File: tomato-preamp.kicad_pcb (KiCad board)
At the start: 2 copper layers, 77 x 75.6 mm, 25 parts, among them J1 IN, J2 OUT, J3.1 +ANODE, J3.2 -ANODE, J4.1 +HEATER, J4.2 -HEATER, U1 6N2P

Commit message: single-layer version
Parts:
- RV1, RV2: moved to B.Cu
- moved R8 25.0 mm to (168.8, 106.4), turned to -90 degrees
- moved C5 25.0 mm to (168.8, 101.3)
- moved C4 10.1 mm to (159.3, 89.7), turned to 180 degrees
- moved RV2 9.84 mm to (139.2, 62.3)
- moved RV1 9.80 mm to (159.8, 62.2)
- moved R6 6.49 mm to (159.4, 79.7)
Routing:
- net Net-(U1B-K): track 19.5 -> 34.2 mm
- net Net-(C6-Pad2): track 19.0 -> 11.9 mm
- net Net-(U1B-G): track 54.0 -> 61.0 mm
- net Net-(U1B-A): track 42.3 -> 45.4 mm
- net Net-(C3-Pad2): track 12.2 -> 10.5 mm
- net Net-(C4-Pad1): track 28.3 -> 27.7 mm
- net GND: vias 44 -> 34

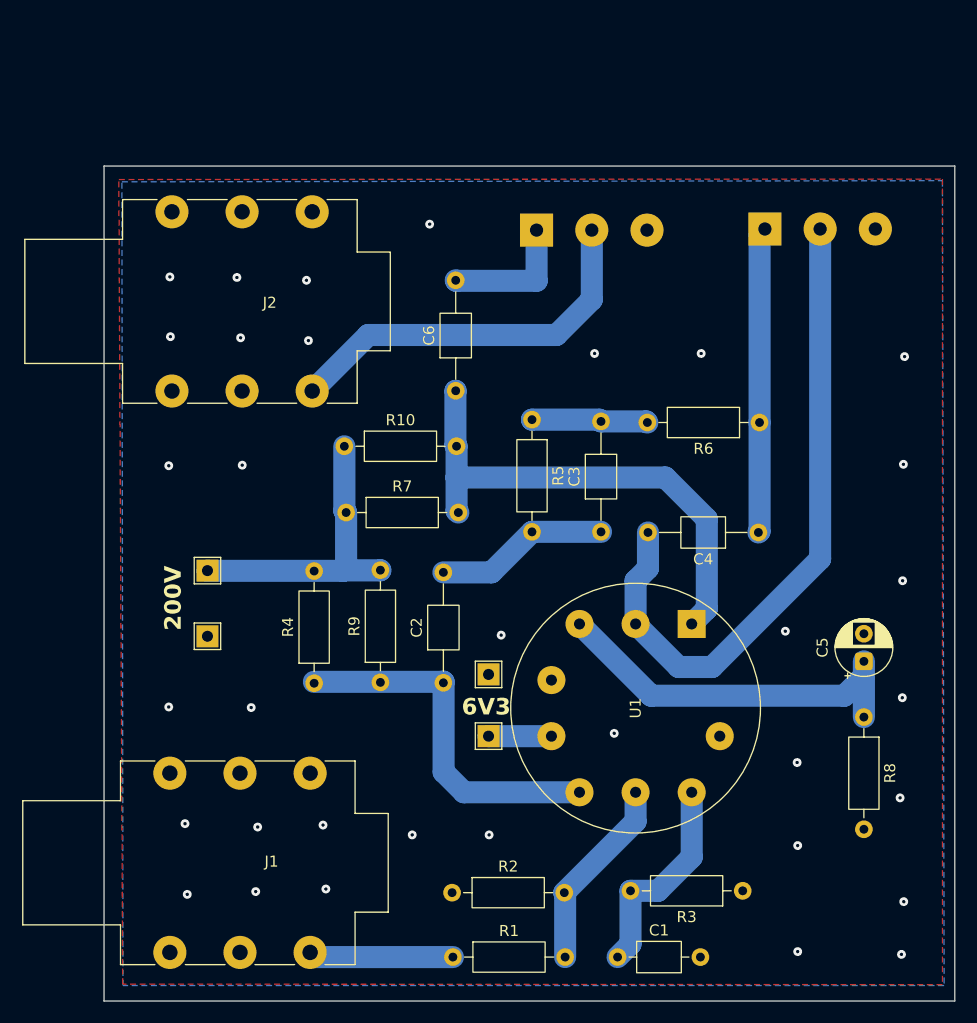
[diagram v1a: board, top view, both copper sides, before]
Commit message: moving potentiometers to the equidistant places
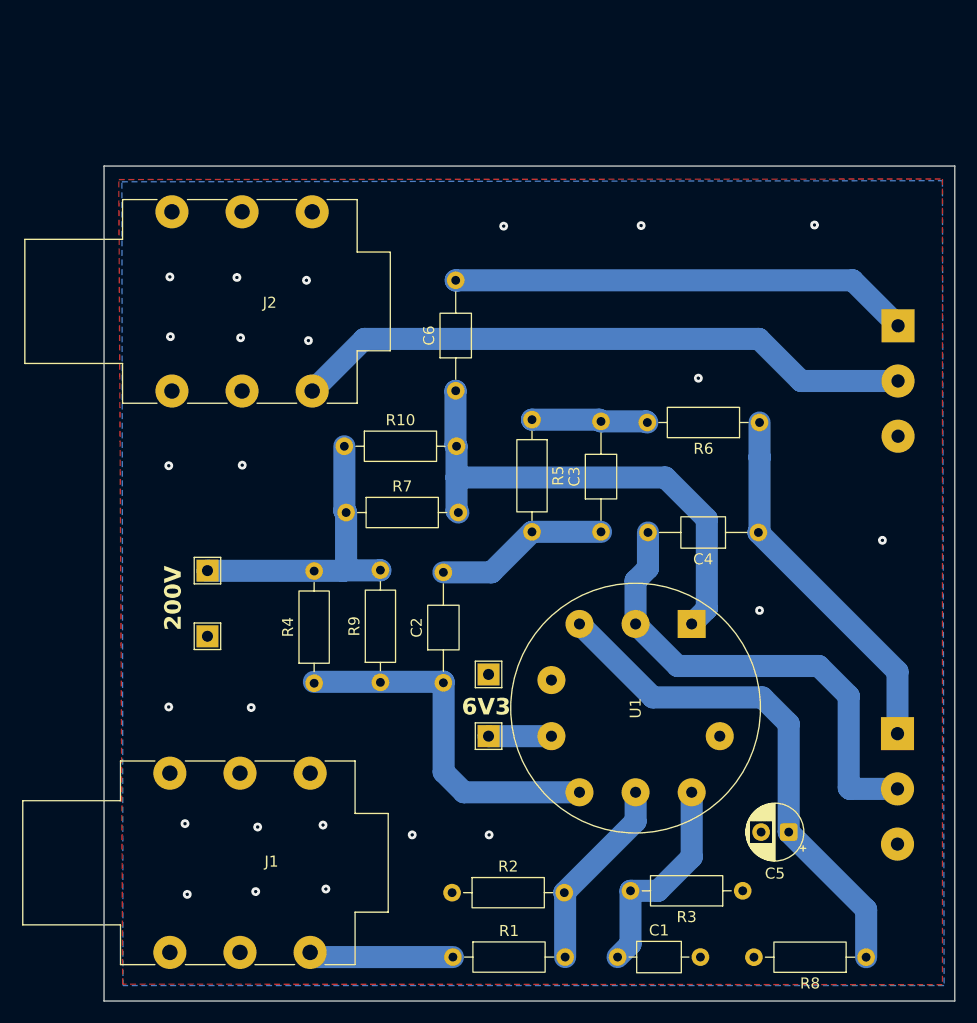
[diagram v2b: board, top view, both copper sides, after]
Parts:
- moved RV1 47.2 mm to (171.9, 107.9), turned to 180 degrees
- moved RV2 33.9 mm to (171.9, 70.9), turned to 180 degrees
- moved R8 21.7 mm to (169.0, 128.1), turned to 180 degrees
- moved C5 16.9 mm to (162.0, 116.8), turned to 180 degrees
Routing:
- net Net-(C6-Pad2): track 11.9 -> 41.8 mm
- net Net-(J2-PadT): track 35.0 -> 56.6 mm
- net Net-(U1B-G): track 61.0 -> 43.5 mm
- net Net-(U1B-K): track 34.2 -> 46.7 mm
- net Net-(C4-Pad1): track 27.7 -> 33.5 mm
- net GND: vias 34 -> 24

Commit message: shorten the traces
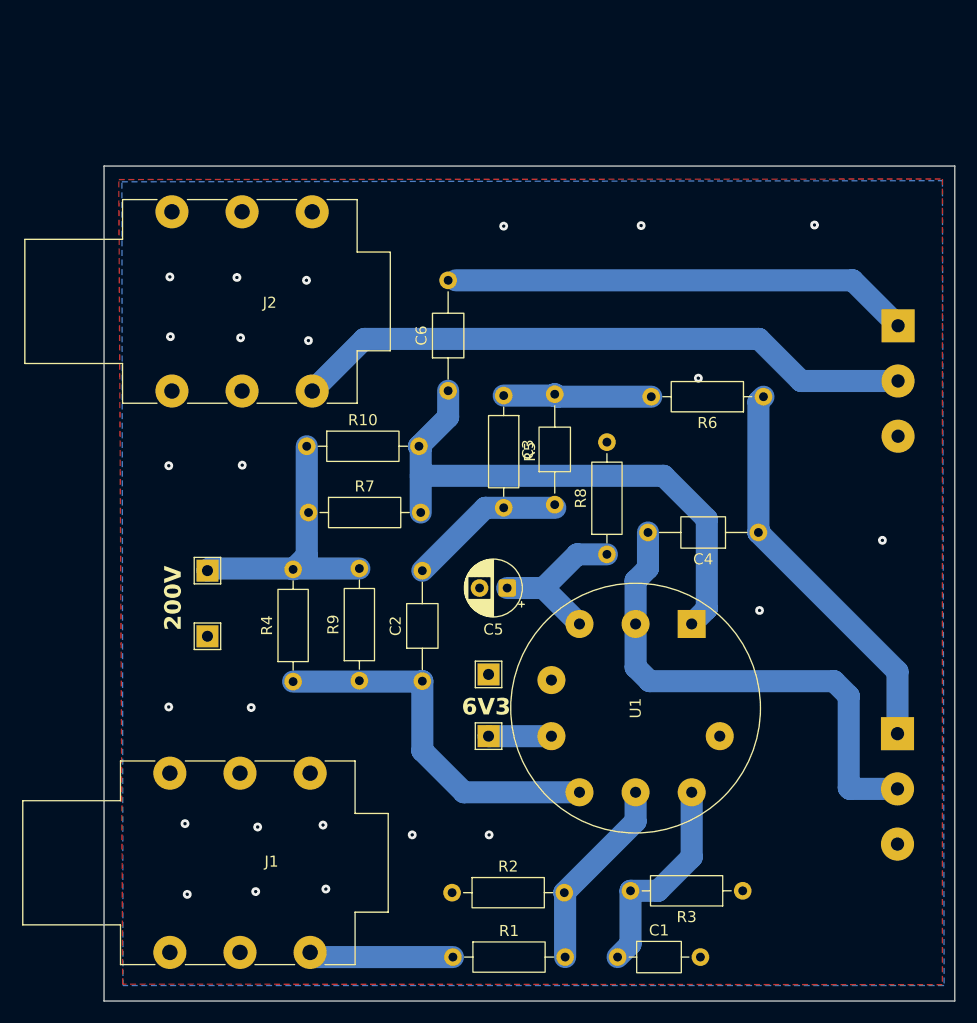
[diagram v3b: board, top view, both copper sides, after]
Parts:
- moved R8 43.4 mm to (145.5, 91.6), turned to 90 degrees
- moved C5 33.7 mm to (136.5, 94.7)
- moved C3 4.86 mm to (140.8, 87.1)
- moved R7 3.40 mm to (118.5, 87.9)
- moved R10 3.40 mm to (118.4, 81.9)
- moved R5 3.36 mm to (136.2, 77.3)
- moved R6 2.36 mm to (159.7, 77.4)
- moved C2 1.91 mm to (128.8, 103.1)
- moved R4 1.91 mm to (117.1, 103.2)
- moved R9 1.91 mm to (123.1, 103.1)
- moved C6 0.69 mm to (131.2, 76.8)
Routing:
- net Net-(U1B-K): track 46.7 -> 14.9 mm
- net Net-(U1B-A): track 45.4 -> 49.8 mm
- net Net-(C3-Pad2): track 10.5 -> 13.5 mm
- net Net-(C4-Pad1): track 33.5 -> 36.1 mm
- net Net-(U1B-G): track 43.5 -> 45.8 mm
- net Net-(J3.1-Pin_1): track 27.0 -> 25.5 mm
- net Net-(C2-Pad2): track 15.8 -> 14.4 mm
- net Net-(U1A-A): track 32.7 -> 33.8 mm

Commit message: a slightly refined board
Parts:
- moved R1 5.81 mm to (131.5, 122.3)
- moved R2 5.77 mm to (131.6, 128.0)
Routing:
- net Net-(J1-PadT): track 13.1 -> 15.1 mm
- net GND: vias 24 -> 22
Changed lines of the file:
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@@
 	(paper "A4")
 	(title_block
-		(title "\"Tomato\" guitar pre-amplifier")
+		(title "\"Adjika\" guitar preamp")
 	)
 	(layers
@@
 	(footprint "Resistor_THT:R_Axial_DIN0207_L6.3mm_D2.5mm_P10.16mm_Horizontal"
 		(layer "F.Cu")
-		(at 131.5212 122.2756)
+		(at 131.572 128.0414)
 		(descr "Resistor, Axial_DIN0207 series, Axial, Horizontal, pin pitch=10.16mm, 0.25W = 1/4W, length*diameter=6.3*2.5mm^2, http://cdn-reichelt.de/documents/datenblatt/B400/1_4W%23YAG.pdf")
 		(tags "Resistor Axial_DIN0207 series Axial Horizontal pin pitch 10.16mm 0.25W = 1/4W length 6.3mm diameter 2.5mm")
@@
 	(footprint "Resistor_THT:R_Axial_DIN0207_L6.3mm_D2.5mm_P10.16mm_Horizontal"
 		(layer "F.Cu")
-		(at 131.597 128.106)
+		(at 131.5466 122.301)
 		(descr "Resistor, Axial_DIN0207 series, Axial, Horizontal, pin pitch=10.16mm, 0.25W = 1/4W, length*diameter=6.3*2.5mm^2, http://cdn-reichelt.de/documents/datenblatt/B400/1_4W%23YAG.pdf")
 		(tags "Resistor Axial_DIN0207 series Axial Horizontal pin pitch 10.16mm 0.25W = 1/4W length 6.3mm diameter 2.5mm")
@@
 	)
 	(via
-		(at 134.874 117.0432)
-		(size 0.8)
-		(drill 0.3)
-		(layers "F.Cu" "B.Cu")
-		(free yes)
-		(net 1)
-	)
-	(via
-		(at 127.9144 117.0432)
-		(size 0.8)
-		(drill 0.3)
-		(layers "F.Cu" "B.Cu")
-		(free yes)
-		(net 1)
-	)
-	(via
 		(at 107.5436 122.428)
 		(size 0.8)
@@
 	)
 	(segment
-		(start 148.137 113.186)
-		(end 148.137 115.8198)
+		(start 141.757 122.1998)
+		(end 141.757 122.3514)
 		(width 2)
 		(layer "B.Cu")
@@
 	)
 	(segment
-		(start 141.757 122.3514)
-		(end 141.6812 122.2756)
+		(start 148.137 115.8198)
+		(end 141.757 122.1998)
 		(width 2)
 		(layer "B.Cu")
@@
 	)
 	(segment
-		(start 148.137 115.8198)
-		(end 141.6812 122.2756)
+		(start 148.137 113.186)
+		(end 148.137 115.8198)
 		(width 2)
 		(layer "B.Cu")
@@
 	)
 	(segment
-		(start 131.597 128.106)
-		(end 119.0896 128.106)
+		(start 126.1624 127.6852)
+		(end 131.5466 122.301)
 		(width 2)
 		(layer "B.Cu")
@@
 	)
 	(segment
-		(start 119.0896 128.106)
-		(end 118.6688 127.6852)
+		(start 118.6688 127.6852)
+		(end 126.1624 127.6852)
 		(width 2)
 		(layer "B.Cu")

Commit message: intermittent
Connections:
- C2 pad 1: Net-(U1A-A) -> /High voltage
- C2 pad 2: Net-(C2-Pad2) -> /High voltage
- C3 pad 1: Net-(C2-Pad2) -> /High voltage
- C4 pad 2: Net-(U1B-G) -> /High voltage
- C6 pad 1: Net-(U1B-A) -> /High voltage
- C6 pad 2: Net-(C6-Pad2) -> /High voltage
- J3.1 pad 1: Net-(J3.1-Pin_1) -> /High voltage
- R10 pad 1: Net-(J3.1-Pin_1) -> /High voltage
- R10 pad 2: Net-(U1B-A) -> /High voltage
- R4 pad 1: Net-(U1A-A) -> /High voltage
- R4 pad 2: Net-(J3.1-Pin_1) -> /High voltage
- R5 pad 2: Net-(C2-Pad2) -> /High voltage
- R7 pad 1: Net-(J3.1-Pin_1) -> /High voltage
- R7 pad 2: Net-(U1B-A) -> /High voltage
- R9 pad 1: Net-(U1A-A) -> /High voltage
- R9 pad 2: Net-(J3.1-Pin_1) -> /High voltage
- RV1 pad 2: Net-(U1B-G) -> /High voltage
- RV2 pad 1: Net-(C6-Pad2) -> /High voltage
- U1 pad 1: Net-(U1B-A) -> /High voltage
- U1 pad 2: Net-(U1B-G) -> /High voltage
- U1 pad 6: Net-(U1A-A) -> /High voltage
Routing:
- net /High voltage: track 0.00 -> 210.5 mm
- net Net-(U1B-A): track 49.8 -> 0.00 mm
- net Net-(U1B-G): track 45.8 -> 0.00 mm
- net Net-(C6-Pad2): track 41.8 -> 0.00 mm
- net Net-(U1A-A): track 33.8 -> 0.00 mm
- net Net-(J3.1-Pin_1): track 25.5 -> 0.00 mm
- net Net-(C2-Pad2): track 14.4 -> 0.00 mm

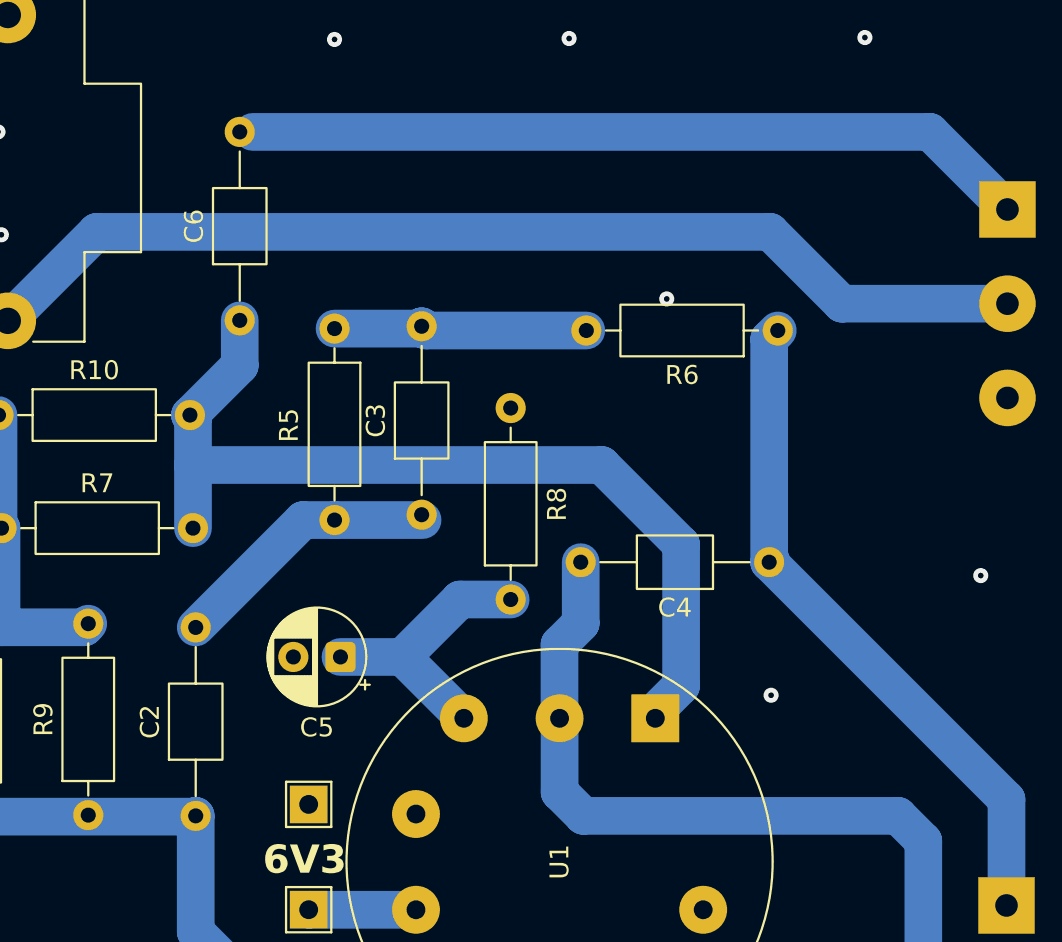
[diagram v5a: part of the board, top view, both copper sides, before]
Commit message: update CBB capacitors footprints
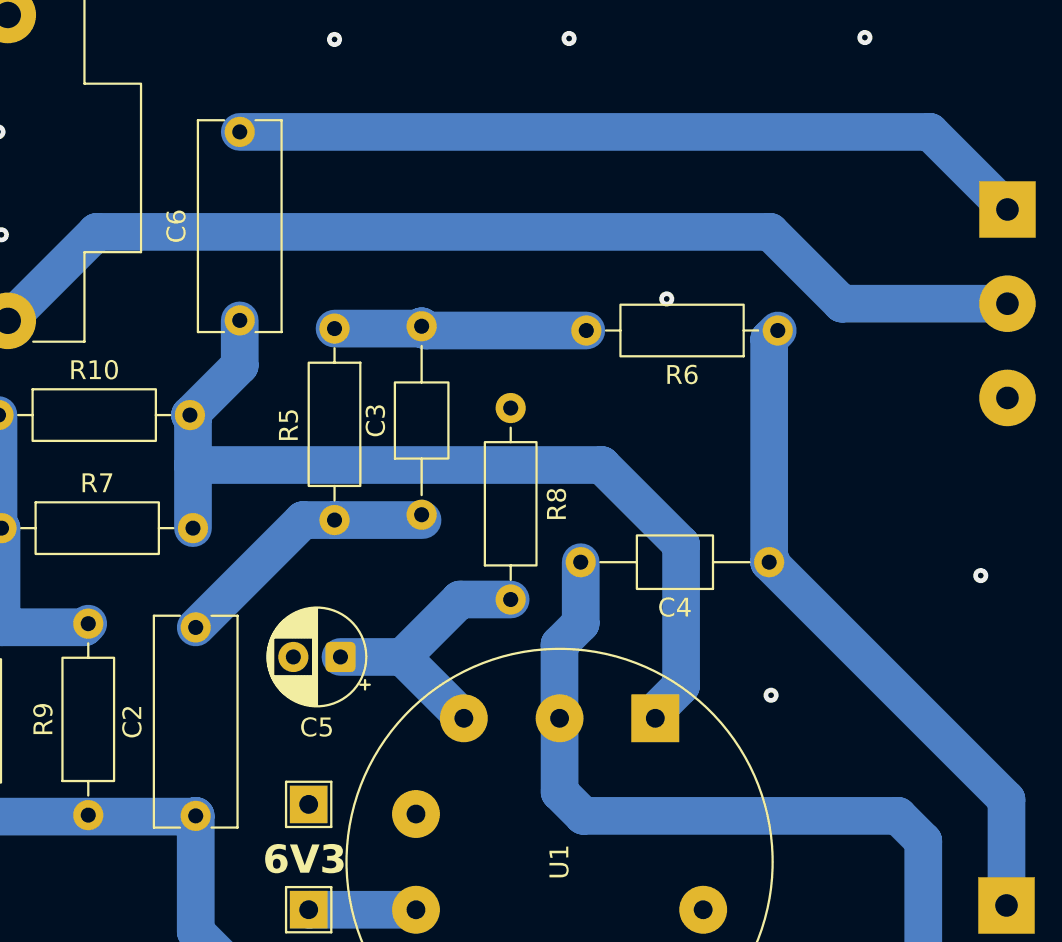
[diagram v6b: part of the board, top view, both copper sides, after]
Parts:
- C2, C6: footprint Capacitor_THT:C_Axial_L3.8mm_D2.6mm_P10.00mm_Horizontal -> Capacitor_THT:C_Rect_L11.0mm_W4.2mm_P10.00mm_MKT
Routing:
- net /High voltage: track 210.5 -> 211.2 mm
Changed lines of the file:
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@@
 		)
 	)
-	(footprint "Capacitor_THT:C_Axial_L3.8mm_D2.6mm_P10.00mm_Horizontal"
+	(footprint "Capacitor_THT:C_Rect_L11.0mm_W4.2mm_P10.00mm_MKT"
 		(layer "F.Cu")
 		(at 128.8288 103.124 90)
-		(descr "C, Axial series, Axial, Horizontal, pin pitch=10mm, length*diameter=3.8*2.6mm^2, http://www.vishay.com/docs/45231/arseries.pdf")
-		(tags "C Axial series Axial Horizontal pin pitch 10mm  length 3.8mm diameter 2.6mm")
+		(descr "C, Rect series, Radial, pin pitch=10.00mm, length*width=11.0*4.2mm^2, Capacitor, https://en.tdk.eu/inf/20/20/db/fc_2009/MKT_B32560_564.pdf")
+		(tags "C Rect series Radial pin pitch 10.00mm length 11.0mm width 4.2mm Capacitor")
 		(property "Reference" "C2"
-			(at 5 -2.42 90)
+			(at 5 -3.35 90)
 			(layer "F.SilkS")
 			(effects
@@
 		)
 		(property "Value" "47n 400V"
-			(at 5 2.42 90)
+			(at 5 3.35 90)
 			(layer "F.Fab")
 			(effects
@@
 		(attr through_hole)
 		(fp_line
-			(start 8.96 0)
-			(end 7.02 0)
-			(stroke
-				(width 0.12)
-				(type solid)
-			)
-			(layer "F.SilkS")
-		)
-		(fp_line
-			(start 1.04 0)
-			(end 2.98 0)
+			(start 10.62 -2.22)
+			(end 10.62 -0.835)
+			(stroke
+				(width 0.12)
+				(type solid)
+			)
+			(layer "F.SilkS")
+		)
+		(fp_line
+			(start -0.62 -2.22)
+			(end 10.62 -2.22)
+			(stroke
+				(width 0.12)
+				(type solid)
+			)
+			(layer "F.SilkS")
+		)
+		(fp_line
+			(start -0.62 -0.835)
+			(end -0.62 -2.22)
+			(stroke
+				(width 0.12)
+				(type solid)
+			)
+			(layer "F.SilkS")
+		)
+		(fp_line
+			(start 10.62 0.835)
+			(end 10.62 2.22)
+			(stroke
+				(width 0.12)
+				(type solid)
+			)
+			(layer "F.SilkS")
+		)
+		(fp_line
+			(start 10.62 2.22)
+			(end -0.62 2.22)
+			(stroke
+				(width 0.12)
+				(type solid)
+			)
+			(layer "F.SilkS")
+		)
+		(fp_line
+			(start -0.62 2.22)
+			(end -0.62 0.835)
 			(stroke
 				(width 0.12)
@@
 		)
 		(fp_rect
-			(start 2.98 -1.42)
-			(end 7.02 1.42)
-			(stroke
-				(width 0.12)
-				(type solid)
-			)
-			(fill no)
-			(layer "F.SilkS")
-		)
-		(fp_rect
-			(start -1.05 -1.55)
-			(end 11.05 1.55)
+			(start -1.05 -2.35)
+			(end 11.05 2.35)
 			(stroke
 				(width 0.05)
@@
 			(layer "F.CrtYd")
 		)
-		(fp_line
-			(start 10 0)
-			(end 6.9 0)
-			(stroke
-				(width 0.1)
-				(type solid)
-			)
-			(layer "F.Fab")
-		)
-		(fp_line
-			(start 0 0)
-			(end 3.1 0)
-			(stroke
-				(width 0.1)
-				(type solid)
-			)
-			(layer "F.Fab")
-		)
 		(fp_rect
-			(start 3.1 -1.3)
-			(end 6.9 1.3)
+			(start -0.5 -2.1)
+			(end 10.5 2.1)
 			(stroke
 				(width 0.1)
@@
 			(effects
 				(font
-					(size 0.76 0.76)
-					(thickness 0.114)
+					(size 1 1)
+					(thickness 0.15)
 				)
 			)
@@
 		)
 		(embedded_fonts no)
-		(model "${KICAD9_3DMODEL_DIR}/Capacitor_THT.3dshapes/C_Axial_L3.8mm_D2.6mm_P10.00mm_Horizontal.step"
+		(model "${KICAD9_3DMODEL_DIR}/Capacitor_THT.3dshapes/C_Rect_L11.0mm_W4.2mm_P10.00mm_MKT.step"
 			(offset
 				(xyz 0 0 0)
@@
 		(embedded_fonts no)
 	)
-	(footprint "Capacitor_THT:C_Axial_L3.8mm_D2.6mm_P10.00mm_Horizontal"
+	(footprint "Capacitor_THT:C_Rect_L11.0mm_W4.2mm_P10.00mm_MKT"
 		(layer "F.Cu")
 		(at 131.1656 76.8312 90)
-		(descr "C, Axial series, Axial, Horizontal, pin pitch=10mm, length*diameter=3.8*2.6mm^2, http://www.vishay.com/docs/45231/arseries.pdf")
-		(tags "C Axial series Axial Horizontal pin pitch 10mm  length 3.8mm diameter 2.6mm")
+		(descr "C, Rect series, Radial, pin pitch=10.00mm, length*width=11.0*4.2mm^2, Capacitor, https://en.tdk.eu/inf/20/20/db/fc_2009/MKT_B32560_564.pdf")
+		(tags "C Rect series Radial pin pitch 10.00mm length 11.0mm width 4.2mm Capacitor")
 		(property "Reference" "C6"
-			(at 5 -2.42 90)
+			(at 5 -3.35 90)
 			(layer "F.SilkS")
 			(effects
@@
 		)
 		(property "Value" "22n 400V"
-			(at 5 2.42 90)
+			(at 5 3.35 90)
 			(layer "F.Fab")
 			(effects
@@
 		(attr through_hole)
 		(fp_line
-			(start 8.96 0)
-			(end 7.02 0)
-			(stroke
-				(width 0.12)
-				(type solid)
-			)
-			(layer "F.SilkS")
-		)
-		(fp_line
-			(start 1.04 0)
-			(end 2.98 0)
+			(start 10.62 -2.22)
+			(end 10.62 -0.835)
+			(stroke
+				(width 0.12)
+				(type solid)
+			)
+			(layer "F.SilkS")
+		)
+		(fp_line
+			(start -0.62 -2.22)
+			(end 10.62 -2.22)
+			(stroke
+				(width 0.12)
+				(type solid)
+			)
+			(layer "F.SilkS")
+		)
+		(fp_line
+			(start -0.62 -0.835)
+			(end -0.62 -2.22)
+			(stroke
+				(width 0.12)
+				(type solid)
+			)
+			(layer "F.SilkS")
+		)
+		(fp_line
+			(start 10.62 0.835)
+			(end 10.62 2.22)
+			(stroke
+				(width 0.12)
+				(type solid)
+			)
+			(layer "F.SilkS")
+		)
+		(fp_line
+			(start 10.62 2.22)
+			(end -0.62 2.22)
+			(stroke
+				(width 0.12)
+				(type solid)
+			)
+			(layer "F.SilkS")
+		)
+		(fp_line
+			(start -0.62 2.22)
+			(end -0.62 0.835)
 			(stroke
 				(width 0.12)
@@
 		)
 		(fp_rect
-			(start 2.98 -1.42)
-			(end 7.02 1.42)
-			(stroke
-				(width 0.12)
-				(type solid)
-			)
-			(fill no)
-			(layer "F.SilkS")
-		)
-		(fp_rect
-			(start -1.05 -1.55)
-			(end 11.05 1.55)
+			(start -1.05 -2.35)
+			(end 11.05 2.35)
 			(stroke
 				(width 0.05)
@@
 			(layer "F.CrtYd")
 		)
-		(fp_line
-			(start 10 0)
-			(end 6.9 0)
-			(stroke
-				(width 0.1)
-				(type solid)
-			)
-			(layer "F.Fab")
-		)
-		(fp_line
-			(start 0 0)
-			(end 3.1 0)
-			(stroke
-				(width 0.1)
-				(type solid)
-			)
-			(layer "F.Fab")
-		)
 		(fp_rect
-			(start 3.1 -1.3)
-			(end 6.9 1.3)
+			(start -0.5 -2.1)
+			(end 10.5 2.1)
 			(stroke
 				(width 0.1)
@@
 			(effects
 				(font
-					(size 0.76 0.76)
-					(thickness 0.114)
+					(size 1 1)
+					(thickness 0.15)
 				)
 			)
@@
 		)
 		(embedded_fonts no)
-		(model "${KICAD9_3DMODEL_DIR}/Capacitor_THT.3dshapes/C_Axial_L3.8mm_D2.6mm_P10.00mm_Horizontal.step"
+		(model "${KICAD9_3DMODEL_DIR}/Capacitor_THT.3dshapes/C_Rect_L11.0mm_W4.2mm_P10.00mm_MKT.step"
 			(offset
 				(xyz 0 0 0)
@@
 	)
 	(segment
+		(start 131.1656 66.8312)
+		(end 167.7876 66.8312)
+		(width 2)
+		(layer "B.Cu")
+		(net 3)
+	)
+	(segment
 		(start 167.4368 104.46172)
 		(end 167.4368 112.776)
@@
 		(width 2)
 		(layer "B.Cu")
-		(net 3)
-	)
-	(segment
-		(start 131.8514 66.8312)
-		(end 167.7876 66.8312)
-		(width 2)
-		(layer "B.Cu")
